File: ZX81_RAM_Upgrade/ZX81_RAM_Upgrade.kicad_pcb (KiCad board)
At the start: 2 copper layers, 24.8 x 36.8 mm, 3 parts, among them J1 Address Expansion, J2 ZX81 RAM Socket, U1 32KB SRAM

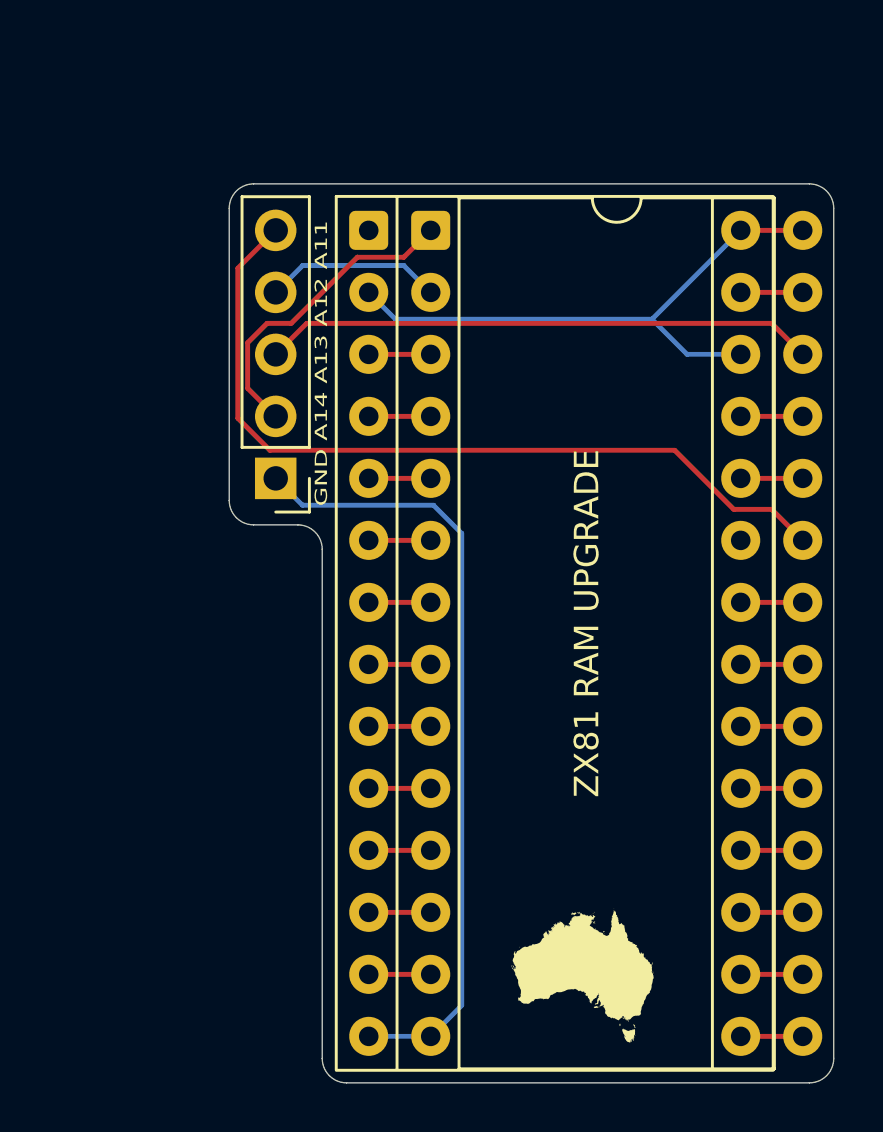
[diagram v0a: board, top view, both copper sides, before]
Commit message: Swapped extension address pins
Now matches order on Issue 1 board: from top, A11/A12/A13/A14
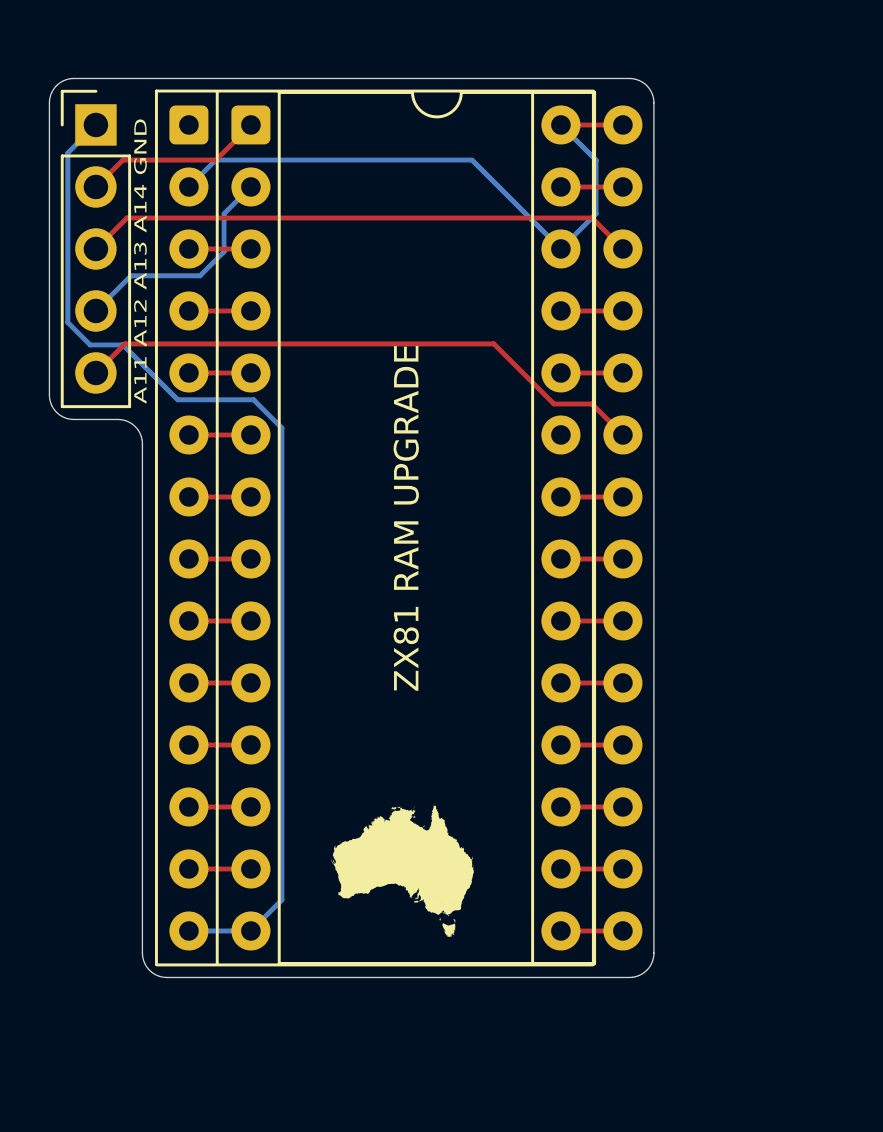
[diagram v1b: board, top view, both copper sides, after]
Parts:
- moved J1 16.2 mm to (78.7, 44.5), turned to 0 degrees
- moved J2 8.54 mm to (82.5, 44.5)
- moved U1 8.54 mm to (85.1, 44.5)
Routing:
- net /GND: track 32.2 -> 42.8 mm
- net /A11: track 33.6 -> 23.6 mm
- net /A14: track 12.9 -> 7.40 mm
- net /A12: track 7.26 -> 9.37 mm
- net /V_{CC}: track 24.0 -> 26.0 mm
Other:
- board text added: "A11 A12 A13 A14 GND"
- board text removed: "GND A14 A13 A12 A11"
